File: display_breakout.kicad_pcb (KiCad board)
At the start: 2 copper layers, 48.9 x 56.6 mm, 32 parts, among them J1 Conn_01x06, U1 MP3216GJE-P, U2 CFAL128128A0-015Y

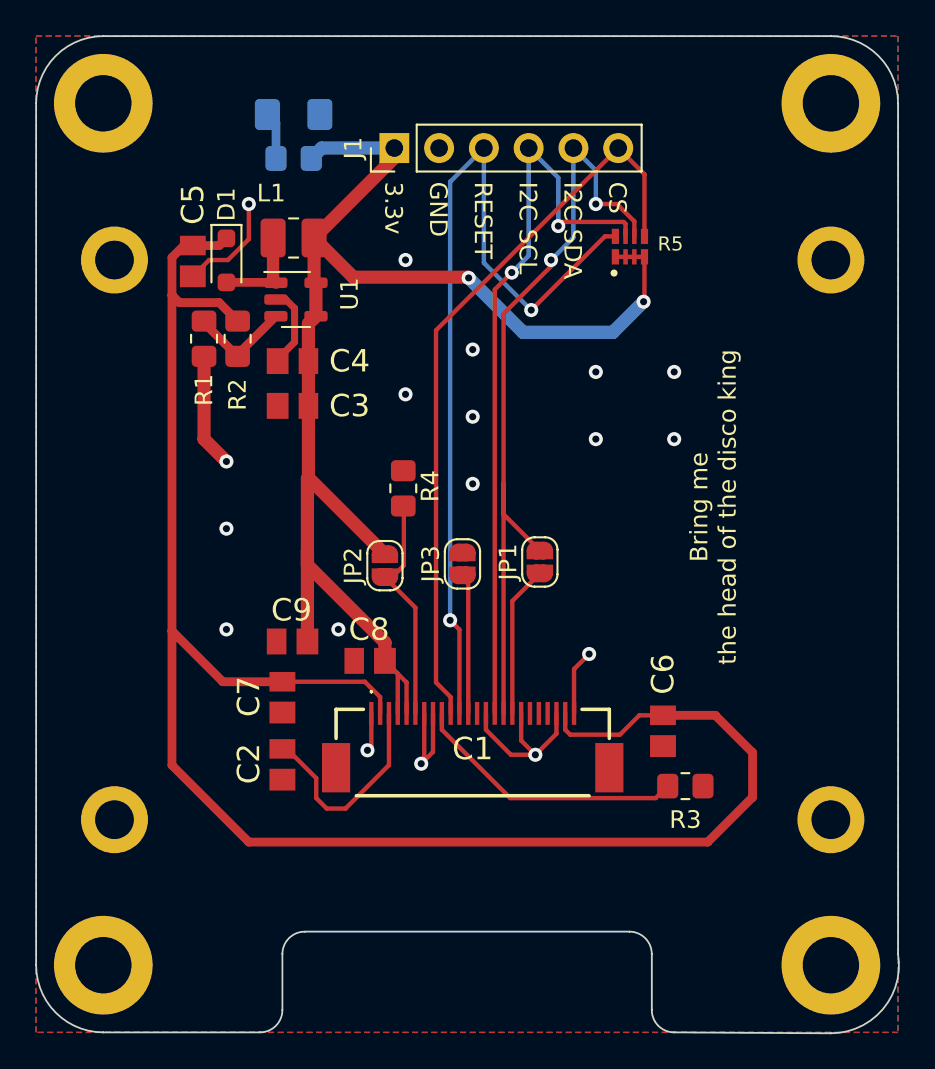
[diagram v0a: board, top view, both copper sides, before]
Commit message: Fix backward display footprint, reroute everything
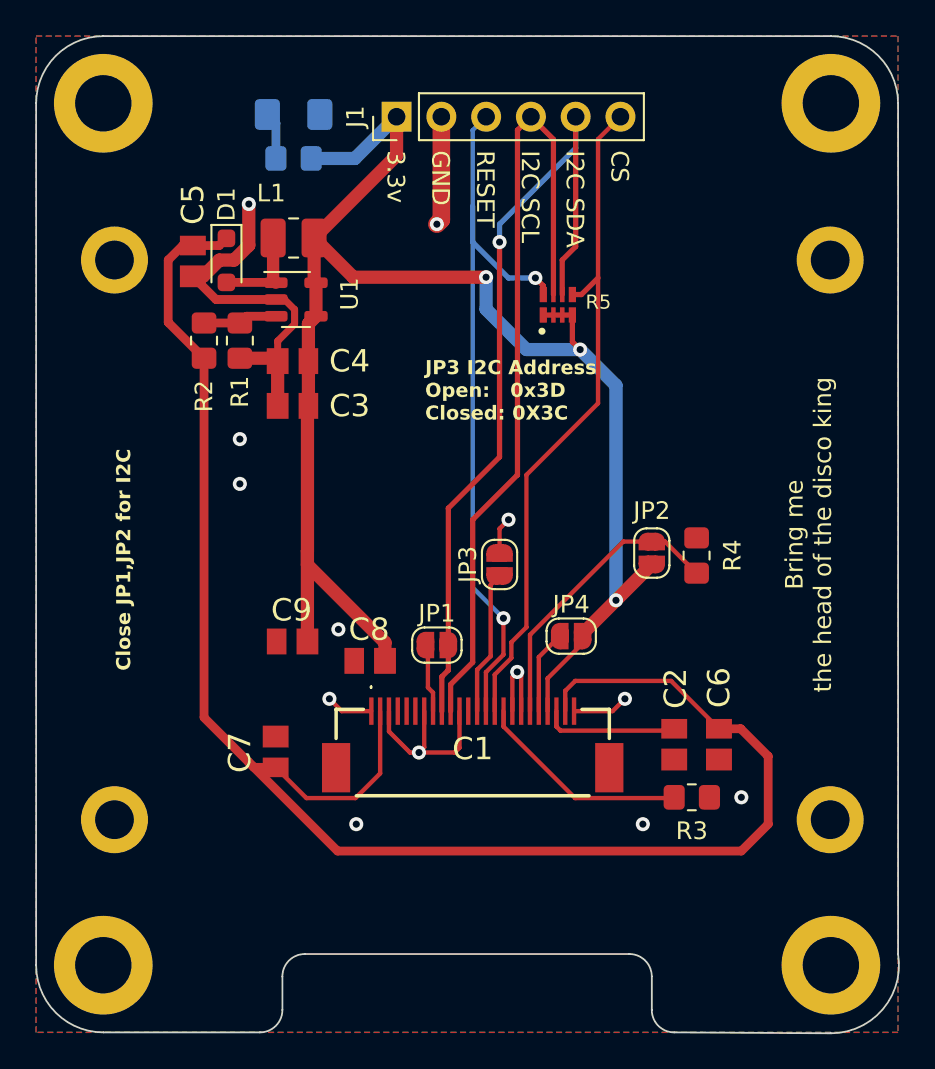
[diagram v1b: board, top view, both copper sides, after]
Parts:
- added JP4: SolderJumper_2_Open, Jumper:SolderJumper-2_P1.3mm_Open_RoundedPad1.0x1.5mm, F.Cu at (137.7, 56.9)
- moved C2 22.3 mm to (143.5, 63.0)
- moved R4 17.1 mm to (144.8, 52.3), turned to -90 degrees
- moved JP2 15.2 mm to (142.2, 52.2), turned to -90 degrees
- moved JP1 7.51 mm to (130.0, 57.4), turned to 0 degrees
- moved R5 5.26 mm to (136.9, 38.1)
- moved C6 3.27 mm to (146.1, 63.0)
- moved C7 3.20 mm to (120.9, 63.5), turned to 90 degrees
- moved JP3 2.10 mm to (133.6, 52.8)
- moved R1 2.03 mm to (118.9, 40.1)
- moved R2 1.91 mm to (116.8, 40.1), turned to 90 degrees
- moved J1 1.78 mm to (127.8, 27.4)
- moved R3 0.73 mm to (144.5, 66.0)
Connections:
- C1 pad 5: +3.3V -> Net-(C1-VDD)
- R4 pad 1: Net-(C1-BS1) -> GND
- R4 pad 2: GND -> Net-(C1-BS1)
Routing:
- net +3.3V: track 81.9 -> 94.2 mm, vias 2 -> 3
- net GND: track 39.0 -> 50.1 mm, vias 18 -> 13
- net RESET: track 49.9 -> 42.7 mm
- net VCC: track 102.3 -> 97.3 mm
- net Net-(C1-VDD): track 0.00 -> 4.75 mm
- net Net-(C1-D2): track 8.59 -> 3.93 mm
- net Net-(C1-VCOMH): track 12.1 -> 7.69 mm
- net SPI_CS: track 42.3 -> 38.5 mm
- net I2C_SCL/SPI_SCK: track 42.7 -> 46.2 mm, vias 2 -> 0
- net Net-(C1-BS1): track 13.2 -> 16.7 mm
- net Net-(C1-IREF): track 15.6 -> 12.3 mm
- net I2C_SDA/SPI_MOSI: track 45.5 -> 47.3 mm, vias 2 -> 1
- net Net-(U1-FB): track 5.96 -> 4.23 mm
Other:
- outline, holes or cut-outs redrawn
- board text added: "CFAL128128A0-015 Breakout v0.2"
- board text added: "Close JP1,JP2 for I2C"
- board text added: "JP3 I2C Address Open: 0x3D Closed: 0X3C"
- board text removed: "CFAL128128A0-015 Breakout v0.1"
